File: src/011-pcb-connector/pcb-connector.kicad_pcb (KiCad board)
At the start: 2 copper layers, 7.8 x 18 mm, 7 parts, among them J1 CONN, J2 CONN

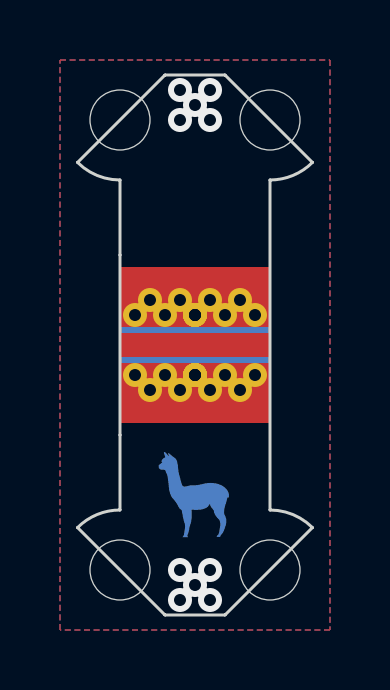
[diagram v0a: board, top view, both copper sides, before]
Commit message: fixing 011-pcb-connector - too wide pcb trace and adding paste layer
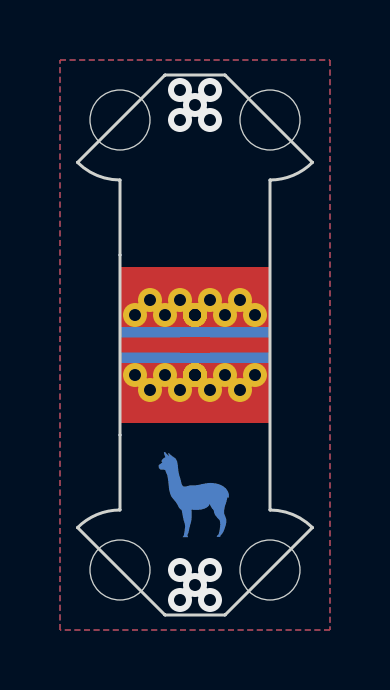
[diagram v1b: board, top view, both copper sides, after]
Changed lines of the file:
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@@
     (0 "F.Cu" signal)
     (31 "B.Cu" signal)
+    (34 "B.Paste" user)
+    (35 "F.Paste" user)
     (36 "B.SilkS" user "B.Silkscreen")
     (37 "F.SilkS" user "F.Silkscreen")
@@
     (stackup
       (layer "F.SilkS" (type "Top Silk Screen") (color "White"))
+      (layer "F.Paste" (type "Top Solder Paste"))
       (layer "F.Mask" (type "Top Solder Mask") (color "Black") (thickness 0.01))
       (layer "F.Cu" (type "copper") (thickness 0.035))
@@
       (layer "B.Cu" (type "copper") (thickness 0.035))
       (layer "B.Mask" (type "Bottom Solder Mask") (color "Black") (thickness 0.01))
+      (layer "B.Paste" (type "Bottom Solder Paste"))
       (layer "B.SilkS" (type "Bottom Silk Screen") (color "White"))
       (copper_finish "None")
@@
     (pad_to_mask_clearance 0)
     (pcbplotparams
-      (layerselection 0x00010f0_ffffffff)
+      (layerselection 0x00010fc_ffffffff)
       (disableapertmacros false)
       (usegerberextensions false)
@@
       ) (layer "F.Mask") (width 0) (fill solid))
     (fp_line (start 0 -3) (end 0 3) (layer "Cmts.User") (width 0.1))
-    (pad "1" smd rect (at -1.5 0 180) (size 3 0.8) (layers "F.Cu")
+    (pad "1" smd rect (at -1.5 0 180) (size 3 0.5) (layers "F.Cu" "F.Paste")
       (net 2 "Net-(J1-Pad1)") (pinfunction "Pin_1") (pintype "passive"))
     (pad "2" thru_hole circle (at -1.5 1 180) (size 0.8 0.8) (drill 0.4) (layers *.Cu) (remove_unused_layers) (keep_end_layers)
@@
       ) (layer "F.Mask") (width 0) (fill solid))
     (fp_line (start 0 -3) (end 0 3) (layer "Cmts.User") (width 0.1))
-    (pad "1" smd rect (at -1.5 0) (size 3 0.8) (layers "F.Cu")
+    (pad "1" smd rect (at -1.5 0) (size 3 0.5) (layers "F.Cu" "F.Paste")
       (net 2 "Net-(J1-Pad1)") (pinfunction "Pin_1") (pintype "passive"))
     (pad "2" thru_hole circle (at -1 1.5) (size 0.8 0.8) (drill 0.4) (layers *.Cu) (remove_unused_layers) (keep_end_layers)
@@
   (via (at 148 90) (size 0.8) (drill 0.4) (layers "F.Cu" "B.Cu") (free) (net 1))
   (via (at 147 75) (size 0.8) (drill 0.4) (layers "F.Cu" "B.Cu") (free) (net 1))
+  (zone (net 0) (net_name "") (layer "F.Cu") (hatch edge 0.508)
+    (connect_pads (clearance 0))
+    (min_thickness 0.254)
+    (keepout (tracks allowed) (vias allowed) (pads allowed) (copperpour not_allowed) (footprints allowed))
+    (fill (thermal_gap 0.508) (thermal_bridge_width 0.508))
+    (polygon
+      (pts
+        (xy 150 83.1)
+        (xy 145 83.1)
+        (xy 145 81.9)
+        (xy 150 81.9)
+      )
+    )
+  )
   (zone (net 1) (net_name "GND") (layers F&B.Cu) (hatch edge 0.508)
     (connect_pads yes (clearance 0.2))

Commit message: fixing 011-pcb-connector - adding revision on PCB
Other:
- board text added: "011 V2"
- board text removed: "011"
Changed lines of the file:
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@@
   (gr_arc (start 145 77) (mid 144.234633 76.847759) (end 143.585786 76.414214) (layer "Edge.Cuts") (width 0.1))
   (gr_line (start 151.414214 76.414214) (end 148.5 73.5) (layer "Edge.Cuts") (width 0.1))
-  (gr_text "011" (at 147.5 78) (layer "B.SilkS")
+  (gr_text "011\nV2" (at 147.5 78.5) (layer "B.SilkS")
     (effects (font (size 1 1) (thickness 0.15)) (justify mirror))
   )
@@
         (xy 151.987696 91.990185)
         (xy 142.987696 91.990185)
-        (xy 142.987696 78.990185)
-        (xy 151.987696 78.990185)
+        (xy 142.987696 79.990185)
+        (xy 151.987696 79.990185)
       )
     )
@@
     (polygon
       (pts
-        (xy 152 79)
-        (xy 149 79)
-        (xy 149 77)
-        (xy 152 77)
+        (xy 152 80)
+        (xy 149 80)
+        (xy 149 76.9)
+        (xy 152 76.9)
       )
     )
@@
     (polygon
       (pts
-        (xy 152 77)
-        (xy 143 77)
+        (xy 152 76.9)
+        (xy 143 76.9)
         (xy 143 73)
         (xy 152 73)
@@
     (polygon
       (pts
-        (xy 146 79)
-        (xy 143 79)
-        (xy 143 77)
-        (xy 146 77)
+        (xy 146 80)
+        (xy 143 80)
+        (xy 143 76.9)
+        (xy 146 76.9)
       )
     )
